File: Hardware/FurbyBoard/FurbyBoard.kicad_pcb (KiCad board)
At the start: 4 copper layers, 68.8 x 74.6 mm, 154 parts, among them J1 USB-C 16P, J11 J_EXP: header de expansión 2 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, J2 BAT+, J3 BAT-, J5 Micro I2S (SD, GND, SCK, WS, 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, J6 FPC 24P 0.5, J7 Frente: IR (emisor ×2, recept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, J8 Inclinación ×3, lengua ×2, al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, J9 Encoder ×3, leva ×2, barriga 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, Q1 SI7615ADN, Q3 AO3400A, SW1 RESET, SW2 BOOT, U1 USBLC6-2SC6, U10 TCA9535PWR, U11 SN74LVC1G17DBVR, U2 BQ24073RGTR, U3 TPS63802DLAR, U4 ESP32-S3-WROOM-1-N16R8, U5 TPS61089RNRR, U6 DRV8231ADSGR, U7 MAX98357AETE+T, U8 ME6211C28M5G-N, U9 ME6211C12M5G-N

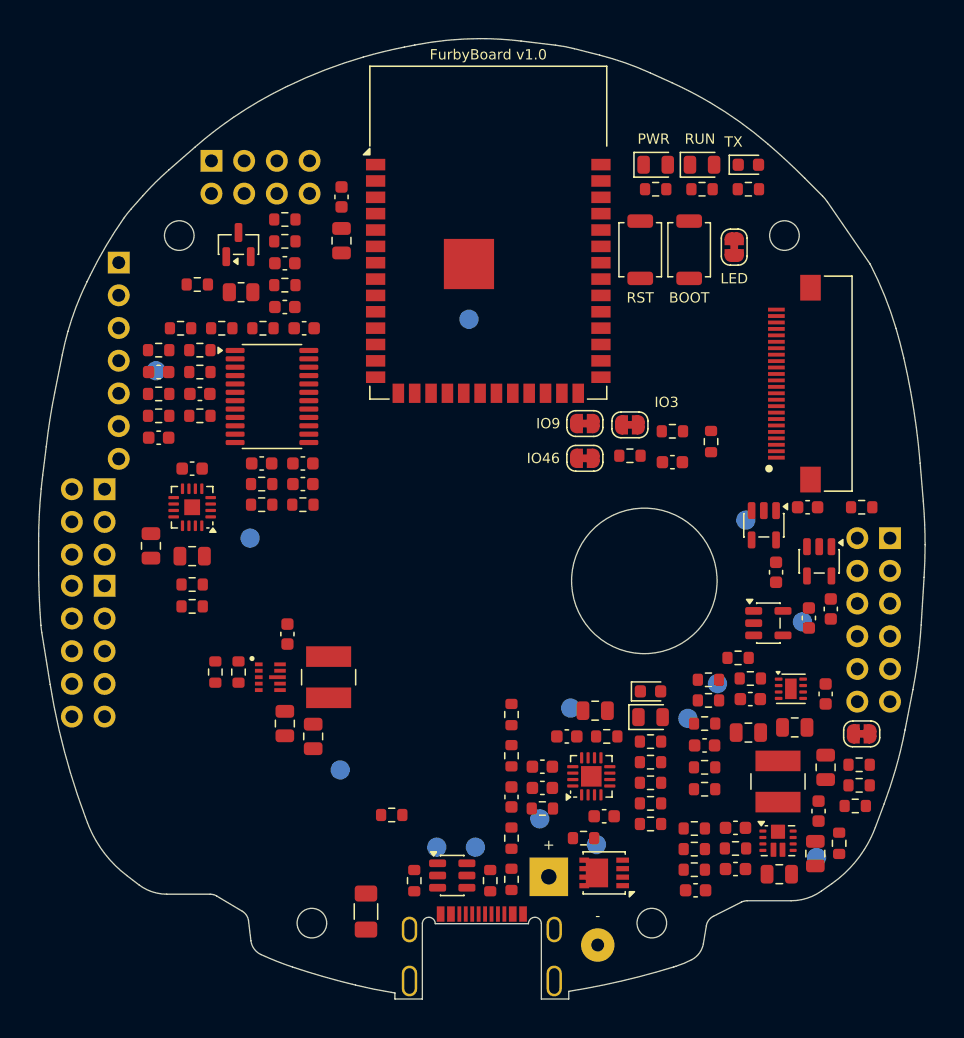
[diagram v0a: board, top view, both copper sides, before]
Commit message: Feature: rutado explícito de potencia y lazos (U5, U3, U2, USB-C auxiliar, tronco de 3V3)
rutas_fijas.py nuevo (DSL por pad con codos a 45°, vías, stubs y polígonos) y gen_pcb.py
con relleno tras recargar y SES opcional. Lazos del elevador (C18 bajo VOUT/GND, SW solo
pad+bobina, VSYS por dos vías), buck-boost (Cin/Cout pegados, SW de 0,6, Kelvin de 3V3 por
B.Cu), cargador (VSYS a C3/C17 y vías, VBUS a C2/C1 y B.Cu, polígono de BAT a C4/Q1, ILIM y
TS por In2 con retorno, EP con 4 vías), VBUS_IN/CC1/CC2 del USB-C y tronco de 3V3 por B.Cu
con ramales. Ajustes de colocación de 0,1-0,5 mm en el elevador, cargador, USB y TP para
las entradas a pad. Puerta D: DRC 0/0 con paridad, revisar-rutado 0 errores (31 avisos:
cuellos en pines de paso fino, asimetrías de pasivos y rodeos documentados), PNG de U5, U3,
U2, U1/J1 y L2 revisados.

Co-Authored-By: Claude Fable 5.1 <noreply@anthropic.com>
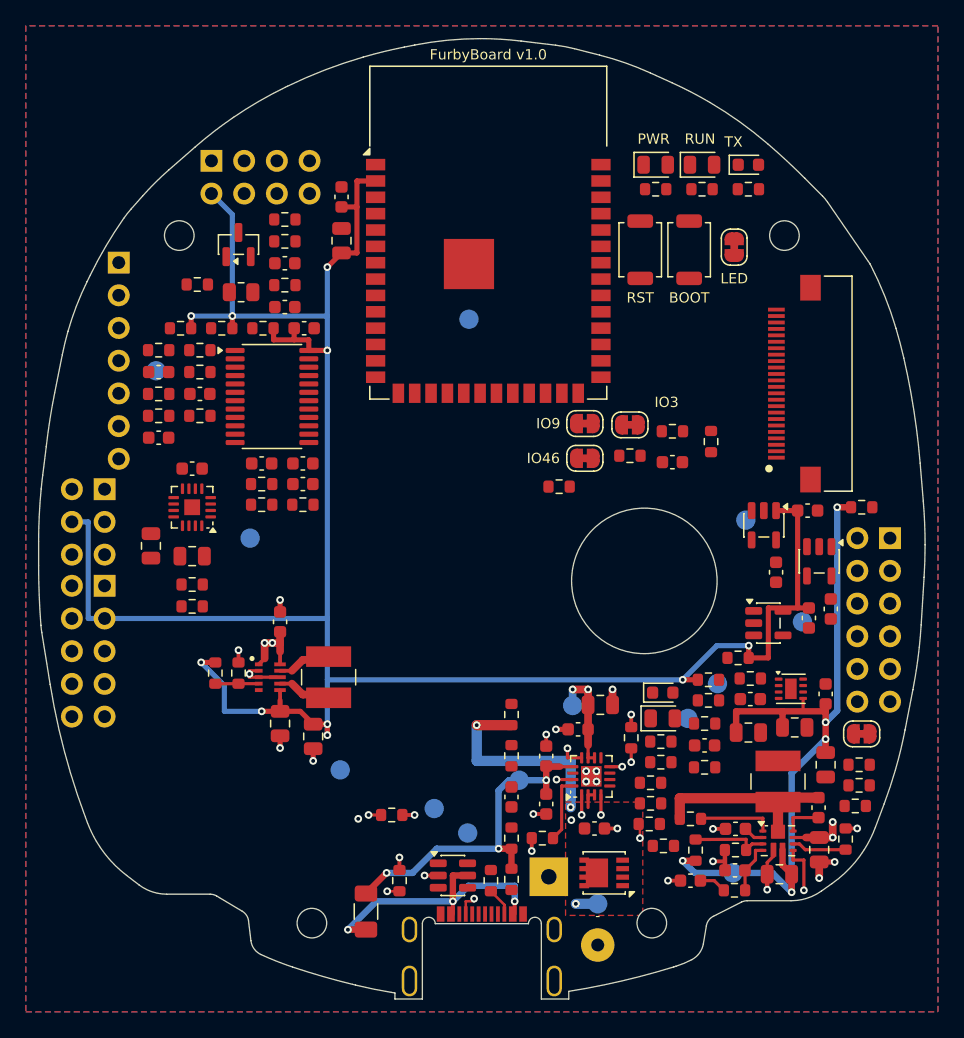
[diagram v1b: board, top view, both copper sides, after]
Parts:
- moved R30 26.1 mm to (152.5, 48.0)
- moved TP7 6.61 mm to (166.0, 78.0)
- moved R12 6.23 mm to (160.6, 75.9)
- moved TP4 4.60 mm to (155.5, 80.4)
- moved R24 3.51 mm to (166.1, 79.3)
- moved TP1 3.40 mm to (149.4, 70.8)
- moved TP2 3.01 mm to (142.8, 73.0)
- moved R4 2.30 mm to (151.2, 75.3), turned to 180 degrees
- moved R5 1.90 mm to (158.1, 67.5), turned to 90 degrees
- moved C1 1.29 mm to (151.5, 72.7), turned to -90 degrees
- moved TP3 1.25 mm to (145.4, 74.9)
- moved C4 1.21 mm to (155.2, 74.5)
- moved R1 1.15 mm to (140.1, 78.6)
- moved C6 1.11 mm to (130.8, 58.5)
- moved C3 1.03 mm to (154.0, 66.8)
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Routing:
- net 3V3: track 0.00 -> 174.4 mm, vias 0 -> 10
- net V6: track 0.00 -> 59.8 mm, vias 0 -> 5
- net GND: track 0.00 -> 32.1 mm, vias 0 -> 31
- net VBUS: track 0.00 -> 27.1 mm, vias 0 -> 3
- net VBUS_IN: track 0.00 -> 22.1 mm, vias 0 -> 3
- net BQ_TS: track 0.00 -> 20.9 mm, vias 0 -> 2
- net BAT: track 0.00 -> 19.6 mm, vias 0 -> 3
- net EN_6V: track 0.00 -> 19.5 mm, vias 0 -> 2
- net VSYS: track 0.00 -> 18.1 mm, vias 0 -> 6
- net BST_SW: track 0.00 -> 13.0 mm
- net CC1: track 0.00 -> 10.9 mm, vias 0 -> 2
- net BQ_ILIM: track 0.00 -> 8.31 mm, vias 0 -> 2
- net BST_FB: track 0.00 -> 6.25 mm
- net BST_FSW: track 0.00 -> 5.82 mm
- net BQ_ISET: track 0.00 -> 5.19 mm
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- added copper zone on F.Cu, net BAT
- added copper zone on B.Cu, net GND
- added copper zone on F.Cu, net GND
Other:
- board text removed: "+"
- board text removed: "BAT"
- board text removed: "BAT-"

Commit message: Feature: rutado del puente H, el amplificador y las vías de VSYS/GND de potencia
U6: V6 a C21/C19/C22/C20 y al pin 5, OUT2 a J9.11 por F.Cu y OUT1 a J9.12 por In2
(pads 11/12 del motor intercambiados en el esquema; ERC 0), IPROPI a R28/TP8 y por In2 a
JP3 fuera del anillo del mecanismo, VREF a C23/R27/R26, EP con 2 vías. U7: VSYS a C26 y
vías, GND al EP, SPK_P/N a J8 en diagonales separadas. Vías de VSYS de L2, R54, R6, C24,
C25 y C17; vías de GND de los pasivos de los dos bloques. Puerta D: DRC 0/0, revisar-rutado
0 errores (48 avisos documentados), PNG de U6, U7 y B.Cu de U6 revisados.

Co-Authored-By: Claude Fable 5.1 <noreply@anthropic.com>
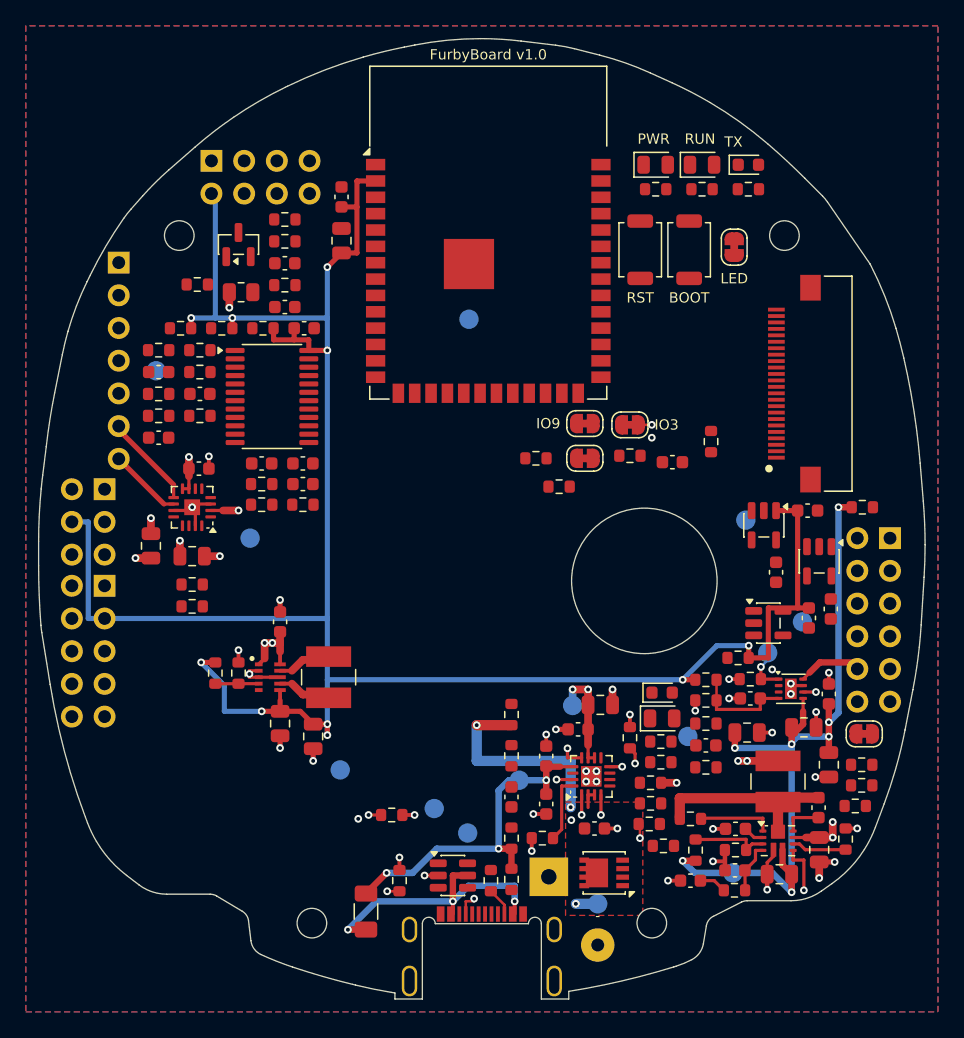
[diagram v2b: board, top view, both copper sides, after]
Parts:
- moved R29 10.8 mm to (150.7, 45.8)
- moved TP8 4.58 mm to (168.7, 60.9)
- moved TP13 1.40 mm to (162.5, 67.4)
- moved C21 0.71 mm to (171.5, 66.7)
- moved C26 0.53 mm to (124.5, 46.6)
- moved C20 0.25 mm to (173.4, 69.6)
- moved C22 0.25 mm to (173.4, 64.1)
- moved JP4 0.20 mm to (176.2, 67.2)
- moved R26 0.20 mm to (163.9, 63.0)
- moved R27 0.20 mm to (163.9, 64.6)
- moved R40 0.20 mm to (176.0, 69.6)
- moved R42 0.20 mm to (176.0, 71.2)
- moved C19 0.10 mm to (167.1, 67.1)
- moved C30 0.10 mm to (163.9, 68.1)
- moved R33 0.10 mm to (163.9, 66.4)
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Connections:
- J9 pad 11: MOT_OUT1 -> MOT_OUT2
- J9 pad 12: MOT_OUT2 -> MOT_OUT1
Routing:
- net IPROPI: track 0.00 -> 28.6 mm, vias 0 -> 2
- net GND: track 32.1 -> 46.1 mm, vias 31 -> 46
- net VSYS: track 18.1 -> 31.1 mm, vias 6 -> 14
- net MOT_VREF: track 0.00 -> 7.98 mm
- net SPK_P: track 0.00 -> 7.03 mm
- net SPK_N: track 0.00 -> 5.72 mm
- net MOT_OUT2: track 0.00 -> 4.75 mm
- net MOT_OUT1: track 0.00 -> 4.52 mm, vias 0 -> 1
- net 3V3: track 174.4 -> 172.7 mm
- net V6: track 59.8 -> 60.8 mm, vias 5 -> 7
- net BQ_ILIM: track 8.31 -> 8.91 mm
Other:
- board text removed: "M1"

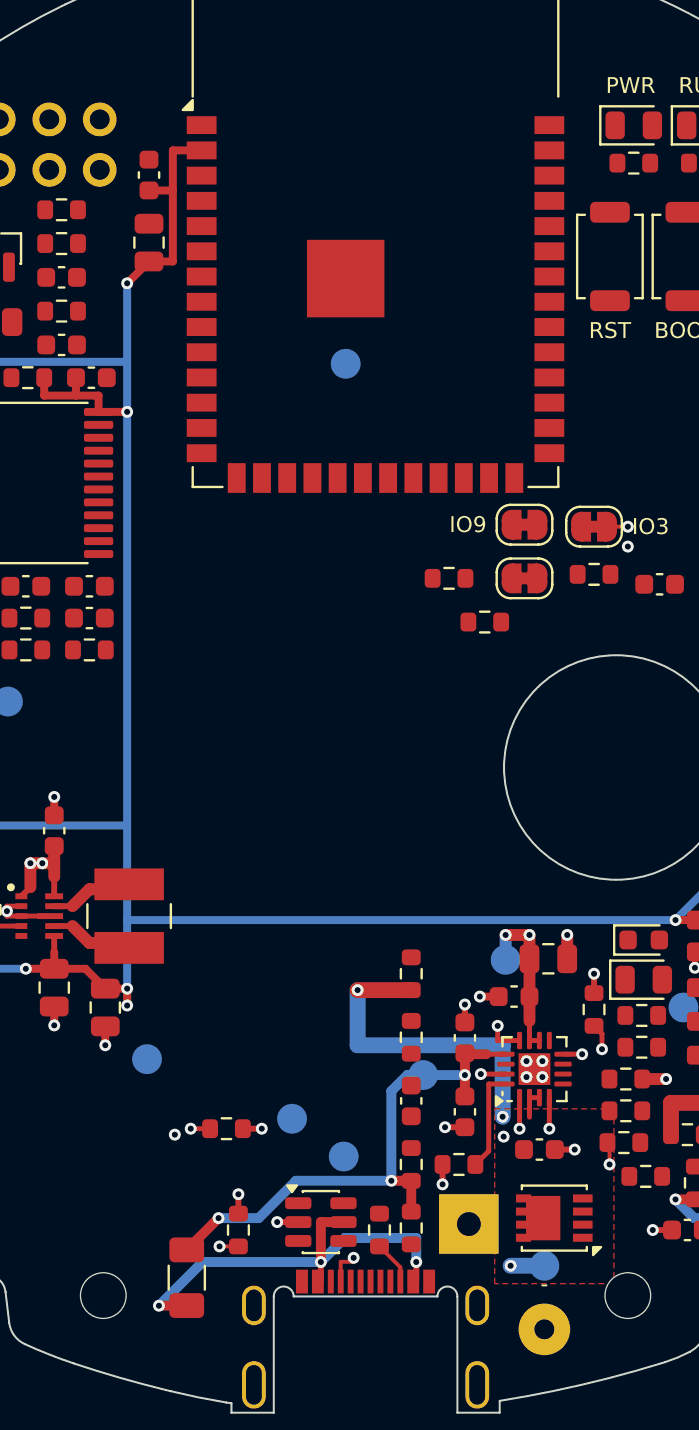
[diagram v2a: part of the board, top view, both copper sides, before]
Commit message: Feature: rutado del par USB y del lado USB-C de la FurbyBoard
Par USB J1 -> U1 -> U4 en F.Cu (0,28/0,15 en el tramo largo, 0,15 en el
campo de pads): D+ por A6 recta y B6 con quiebro, D- por B7 recta y A7
con una vía de 0,45 por B.Cu hasta la salida del pin 3; retorno de GND a
menos de 1 mm de cada vía. U1 (USBLC6) es de paso, así que los pines 6-1
y 4-3 van unidos bajo el cuerpo y VBUS_IN entra al pin 5 y baja a In2
por una vía bajo U1; A4/B9 y A9/B4 bajan a In2 con sus vías y llegan a
F1 por la fila y -115,9 sin cruzar BQ_TS. CC1 por In2 (fila y -120,8) a
R1 y CC2 por B.Cu (fila y -120,9) a R2. TP3 sobre la pista de D- en B y
TP2 sobre una vía de D+ a la entrada del módulo (U4.14).

Colocación: U1 0,1 mm al oeste, R1/R2 al oeste de U1, R10/R11/R4 0,4 mm
al este, TP3 bajo U1; vías térmicas del módulo (U4:41) declaradas.

Puerta D: DRC 0 con paridad 0, revisar-rutado 0 errores (53 avisos
documentados), PNG revisados de las zonas U1 (F, B, In2) y J1 (F).

Co-Authored-By: Claude Fable 5.1 <noreply@anthropic.com>
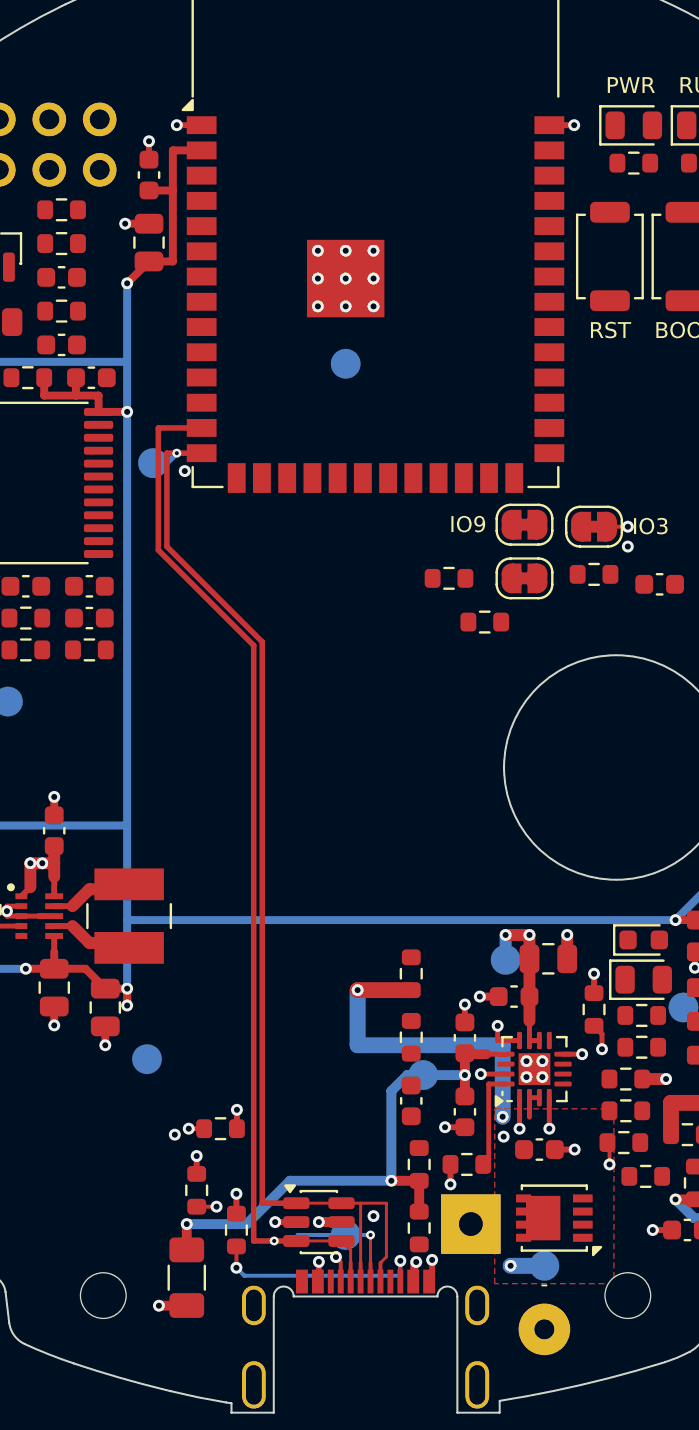
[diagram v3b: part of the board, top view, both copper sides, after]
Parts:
- moved TP2 33.7 mm to (135.8, 40.0)
- moved R2 7.20 mm to (140.0, 78.6)
- moved TP3 3.95 mm to (145.5, 78.8)
- moved R1 2.90 mm to (138.0, 76.6)
- moved R4 0.40 mm to (151.6, 75.3)
- moved R10 0.40 mm to (149.2, 75.3)
- moved R11 0.40 mm to (149.2, 78.5)
- moved RT1 0.30 mm to (139.2, 73.5)
- moved J2 0.10 mm to (151.8, 78.3)
- moved U1 0.10 mm to (144.2, 78.2)
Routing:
- net USB_DN: track 0.00 -> 59.1 mm, vias 0 -> 2
- net USB_DP: track 0.00 -> 57.2 mm, vias 0 -> 1
- net VBUS_IN: track 22.1 -> 31.5 mm, vias 3 -> 4
- net CC2: track 2.20 -> 11.3 mm, vias 0 -> 2
- net GND: track 46.1 -> 52.8 mm, vias 46 -> 63
- net VBUS: track 27.1 -> 28.3 mm
